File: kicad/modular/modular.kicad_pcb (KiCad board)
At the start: 2 copper layers, 50 x 36 mm, 55 parts, among them J1 CONN_PWR, J2 HEADER, J3 HEADER, U1 LM317, U2 LM337, U3 OPA4197, U4 REF5010

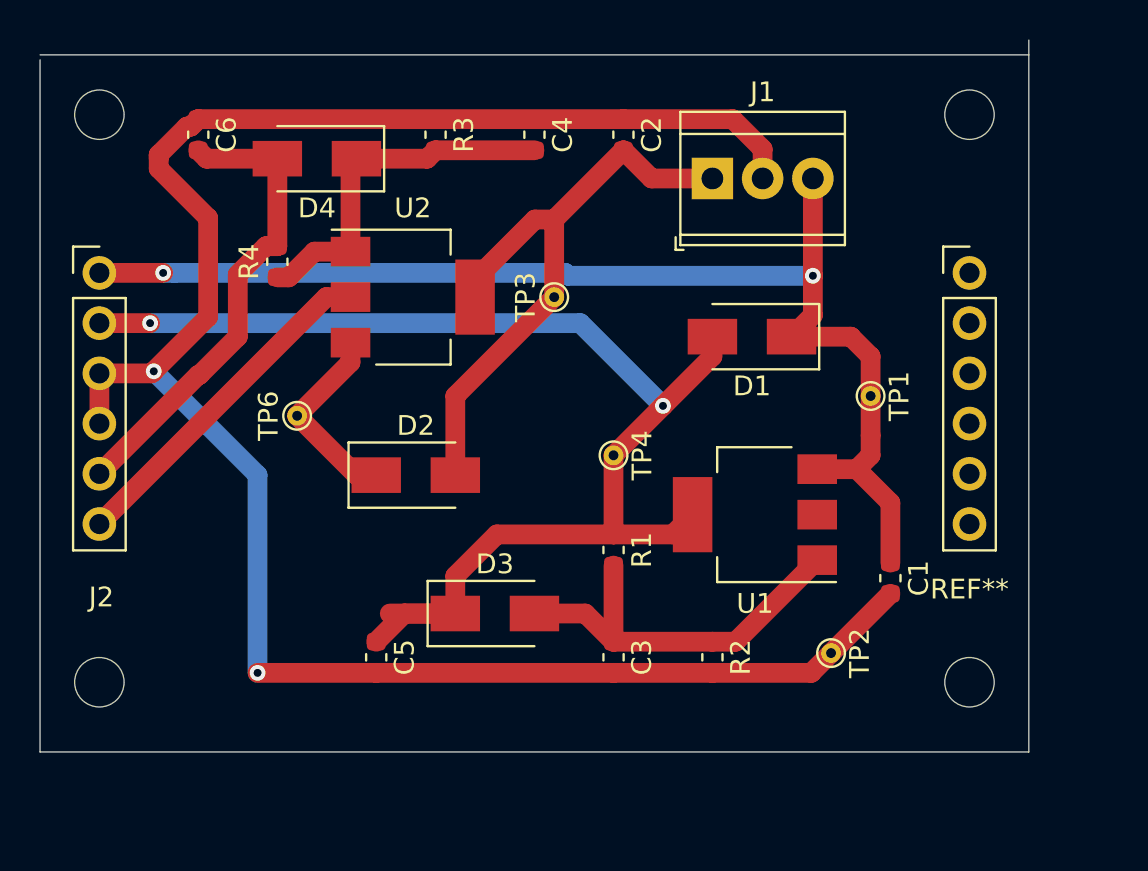
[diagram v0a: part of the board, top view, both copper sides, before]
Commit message: completed pcb design of power board
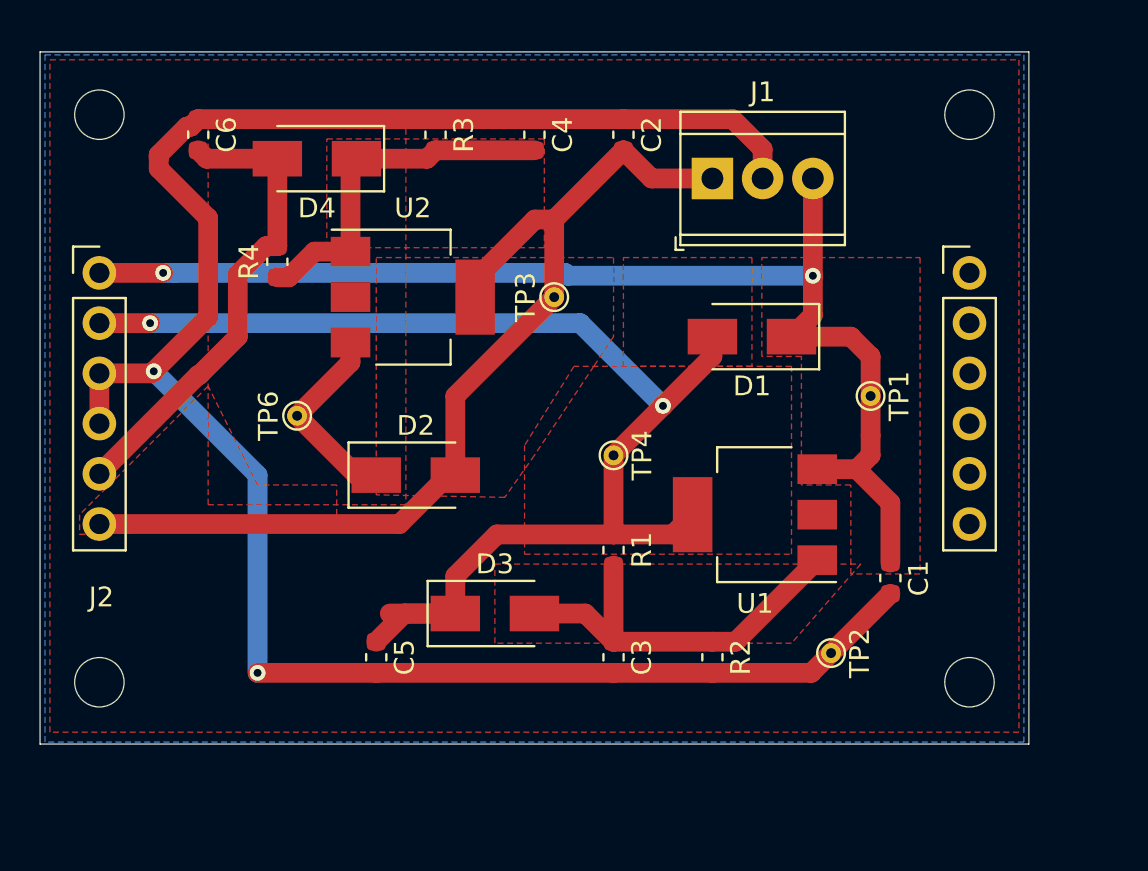
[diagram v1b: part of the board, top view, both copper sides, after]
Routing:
- net -15V: track 48.6 -> 50.2 mm
- added copper zone on F.Cu, net +12V
- added copper zone on F.Cu, net +15V
- added copper zone on F.Cu, net -12V
- added copper zone on F.Cu, net -15V
- added copper zone on B.Cu, net GND
- added copper zone on F.Cu, net GND
- added copper zone on F.Cu, net Net-(C3-Pad1)
- added copper zone on F.Cu, net Net-(C4-Pad2)
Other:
- board size 50 x 36 mm -> 50 x 35 mm
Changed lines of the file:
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@@
     (thickness 1.6)
     (drawings 4)
-    (tracks 102)
+    (tracks 103)
     (zones 0)
     (modules 55)
@@
   (layers
     (0 F.Cu signal)
-    (31 B.Cu signal)
+    (31 B.Cu signal hide)
     (32 B.Adhes user)
     (33 F.Adhes user)
@@
       (effects (font (size 1 1) (thickness 0.15)))
     )
-    (fp_text user REF** (at 44 16) (layer F.SilkS)
-      (effects (font (size 1 1) (thickness 0.15)))
-    )
     (fp_text user %R (at 0.3 -8) (layer F.Fab)
       (effects (font (size 1 1) (thickness 0.15)))
@@
     )
   )
-  (gr_line (start 40 26.75) (end 90 26.75) (layer Edge.Cuts) (width 0.05))
-  (gr_line (start 40 62) (end 40 27) (layer Edge.Cuts) (width 0.05))
-  (gr_line (start 90 62) (end 40 62) (layer Edge.Cuts) (width 0.05))
-  (gr_line (start 90 26) (end 90 62) (layer Edge.Cuts) (width 0.05))
+  (gr_line (start 40 26.6) (end 90 26.6) (layer Edge.Cuts) (width 0.05))
+  (gr_line (start 40 61.6) (end 40 26.6) (layer Edge.Cuts) (width 0.05))
+  (gr_line (start 90 61.6) (end 40 61.6) (layer Edge.Cuts) (width 0.05))
+  (gr_line (start 90 26.6) (end 90 61.6) (layer Edge.Cuts) (width 0.05))
   (segment (start 81.3 47.7) (end 82 47) (width 1) (layer F.Cu) (net 1))
   (segment (start 79.3 47.7) (end 81.3 47.7) (width 1) (layer F.Cu) (net 1))
@@
   (segment (start 70.925 33) (end 69.5 31.575) (width 1) (layer F.Cu) (net 3))
   (segment (start 74 33) (end 70.925 33) (width 1) (layer F.Cu) (net 3))
-  (segment (start 54.475001 39) (end 55.7 39) (width 1) (layer F.Cu) (net 3))
-  (segment (start 43 50.475001) (end 54.475001 39) (width 1) (layer F.Cu) (net 3))
+  (segment (start 58.174999 50.475001) (end 60.65 48) (width 1) (layer F.Cu) (net 3))
+  (segment (start 60.65 48) (end 61 48) (width 1) (layer F.Cu) (net 3))
+  (segment (start 43 50.475001) (end 58.174999 50.475001) (width 1) (layer F.Cu) (net 3))
   (segment (start 69 52.575) (end 69 56.425) (width 1) (layer F.Cu) (net 4))
   (segment (start 69 56.425) (end 74 56.425) (width 1) (layer F.Cu) (net 4))
@@
   (segment (start 51.425 36.425) (end 52 36.425) (width 1) (layer F.Cu) (net 7))
   (segment (start 50 41) (end 50 37.85) (width 1) (layer F.Cu) (net 7))
+  (zone (net 2) (net_name GND) (layer B.Cu) (hatch edge 0.508)
+    (connect_pads (clearance 0.508))
+    (min_thickness 0.254)
+    (fill yes (arc_segments 32) (thermal_gap 0.508) (thermal_bridge_width 0.508))
+    (polygon
+      (pts
+        (xy 40.25 26.75) (xy 89.75 26.75) (xy 89.75 61.5) (xy 40.25 61.5)
+      )
+    )
+  )
+  (zone (net 5) (net_name "Net-(C4-Pad2)") (layer F.Cu) (hatch edge 0.508)
+    (priority 5)
+    (connect_pads (clearance 0.508))
+    (min_thickness 0.254)
+    (fill yes (arc_segments 32) (thermal_gap 0.508) (thermal_bridge_width 0.508))
+    (polygon
+      (pts
+        (xy 54.5 31) (xy 65.5 31) (xy 65.5 36.5) (xy 54.5 36.5)
+      )
+    )
+  )
+  (zone (net 3) (net_name -15V) (layer F.Cu) (hatch edge 0.508)
+    (priority 4)
+    (connect_pads (clearance 0.508))
+    (min_thickness 0.254)
+    (fill yes (arc_segments 32) (thermal_gap 0.508) (thermal_bridge_width 0.508) (smoothing chamfer))
+    (polygon
+      (pts
+        (xy 57 37) (xy 69 37) (xy 69 41) (xy 68 42.5) (xy 65 47)
+        (xy 63.5 49.125) (xy 57 49)
+      )
+    )
+  )
+  (zone (net 4) (net_name "Net-(C3-Pad1)") (layer F.Cu) (hatch edge 0.508)
+    (priority 5)
+    (connect_pads (clearance 0.508))
+    (min_thickness 0.254)
+    (fill yes (arc_segments 32) (thermal_gap 0.508) (thermal_bridge_width 0.508) (smoothing chamfer))
+    (polygon
+      (pts
+        (xy 63 52.5) (xy 81.5 52.5) (xy 78 56.5) (xy 63 56.5)
+      )
+    )
+  )
+  (zone (net 6) (net_name +12V) (layer F.Cu) (hatch edge 0.508)
+    (priority 2)
+    (connect_pads (clearance 0.508))
+    (min_thickness 0.254)
+    (fill yes (arc_segments 32) (thermal_gap 0.508) (thermal_bridge_width 0.508) (smoothing chamfer))
+    (polygon
+      (pts
+        (xy 78 52) (xy 78 42.5) (xy 76 42.5) (xy 67 42.5) (xy 64.5 46.5)
+        (xy 64.5 52)
+      )
+    )
+  )
+  (zone (net 6) (net_name +12V) (layer F.Cu) (hatch edge 0.508)
+    (priority 2)
+    (connect_pads (clearance 0.508))
+    (min_thickness 0.254)
+    (fill yes (arc_segments 32) (thermal_gap 0.508) (thermal_bridge_width 0.508) (smoothing chamfer))
+    (polygon
+      (pts
+        (xy 69.5 37) (xy 76 37) (xy 76 42.5) (xy 69.5 42.5)
+      )
+    )
+  )
+  (zone (net 1) (net_name +15V) (layer F.Cu) (hatch edge 0.508)
+    (priority 4)
+    (connect_pads (clearance 0.508))
+    (min_thickness 0.254)
+    (fill yes (arc_segments 32) (thermal_gap 0.508) (thermal_bridge_width 0.508) (smoothing chamfer))
+    (polygon
+      (pts
+        (xy 76.5 37) (xy 84.5 37) (xy 84.5 53) (xy 81 53) (xy 81 48.5)
+        (xy 78.5 48.5) (xy 78.5 42) (xy 76.5 42)
+      )
+    )
+  )
+  (zone (net 2) (net_name GND) (layer F.Cu) (hatch edge 0.508)
+    (connect_pads (clearance 0.508))
+    (min_thickness 0.254)
+    (fill yes (arc_segments 32) (thermal_gap 0.508) (thermal_bridge_width 0.508) (smoothing chamfer))
+    (polygon
+      (pts
+        (xy 40.5 27) (xy 89.5 27) (xy 89.5 61) (xy 40.5 61)
+      )
+    )
+  )
+  (zone (net 7) (net_name -12V) (layer F.Cu) (hatch edge 0.508)
+    (priority 10)
+    (connect_pads (clearance 0.508))
+    (min_thickness 0.254)
+    (fill yes (arc_segments 32) (thermal_gap 0.508) (thermal_bridge_width 0.508) (smoothing chamfer))
+    (polygon
+      (pts
+        (xy 48.5 30) (xy 58.5 30) (xy 58.5 49.5) (xy 48.5 49.5)
+      )
+    )
+  )
+  (zone (net 3) (net_name -15V) (layer F.Cu) (hatch edge 0.508)
+    (priority 1)
+    (connect_pads (clearance 0.508))
+    (min_thickness 0.254)
+    (fill yes (arc_segments 32) (thermal_gap 0.508) (thermal_bridge_width 0.508) (smoothing chamfer))
+    (polygon
+      (pts
+        (xy 42 51) (xy 55 50.5) (xy 55 48.5) (xy 51 48.5) (xy 48.5 43.5)
+        (xy 42 50)
+      )
+    )
+  )
 )

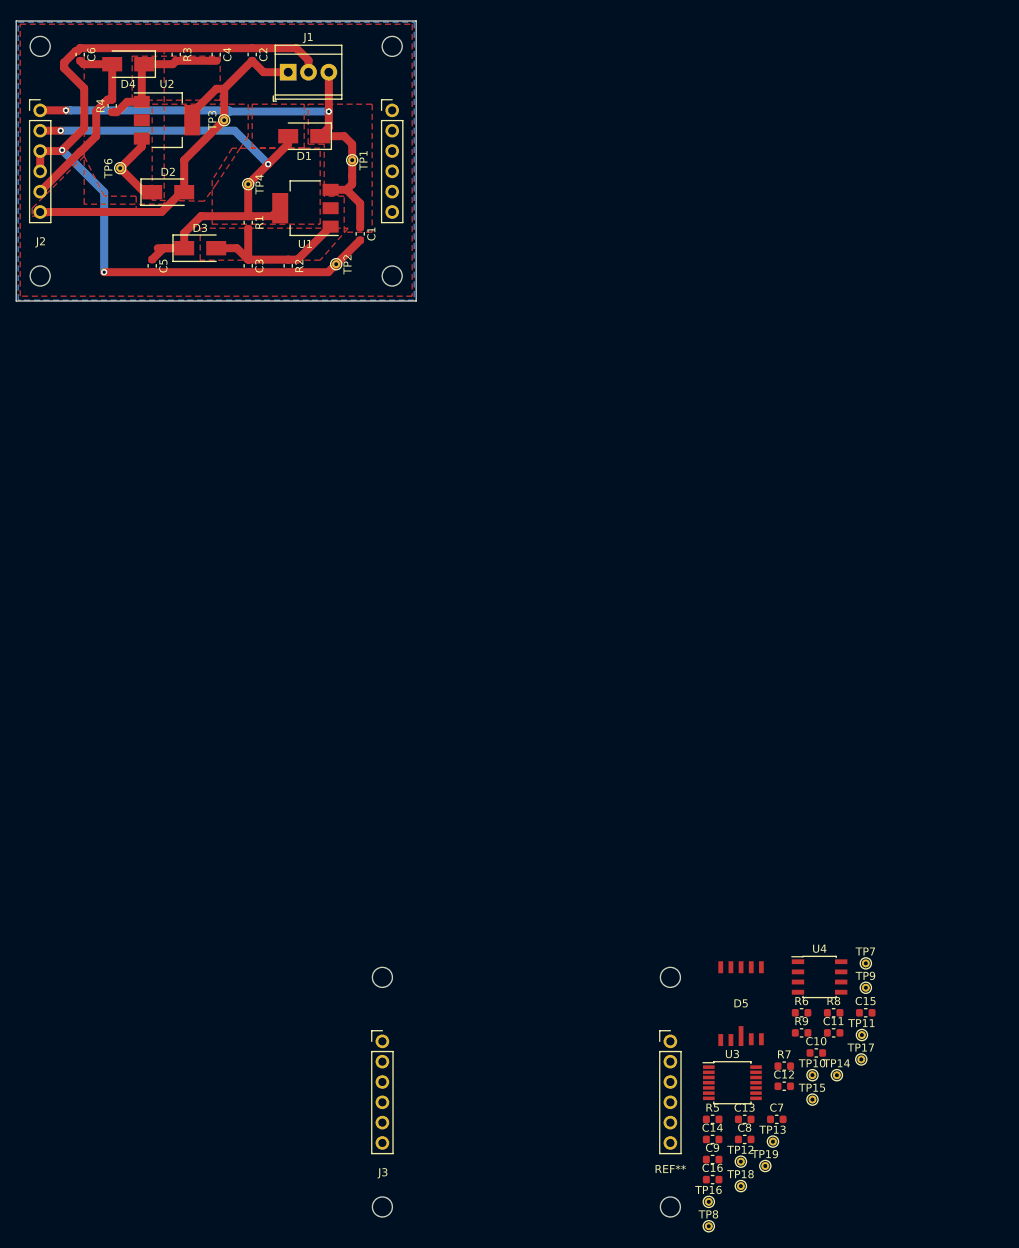
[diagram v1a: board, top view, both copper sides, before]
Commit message: updated detector board footprints, added edge cuts
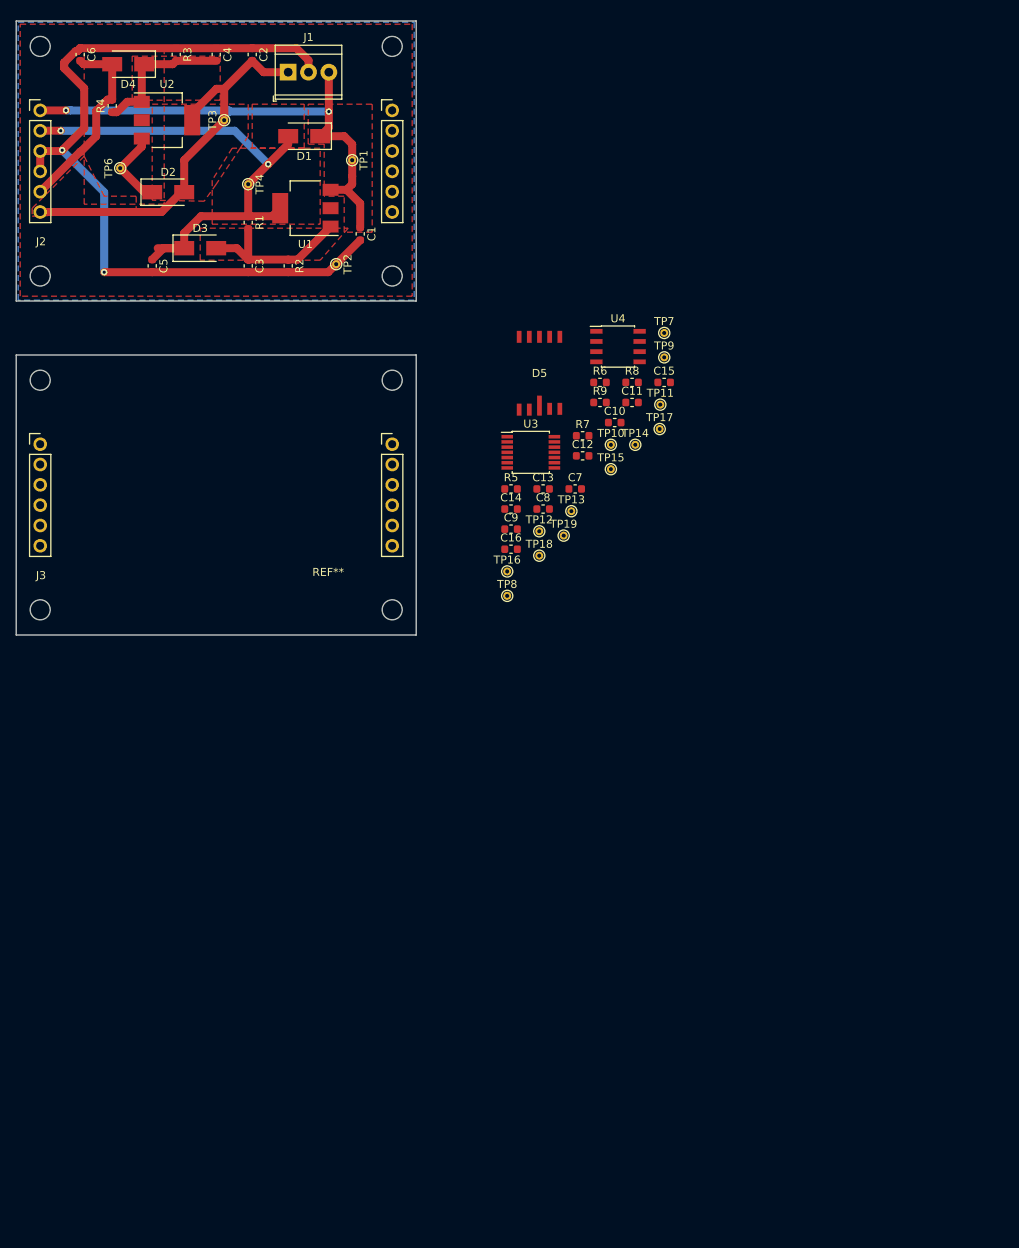
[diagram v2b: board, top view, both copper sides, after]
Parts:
- J2: value HEADER -> Power
- moved J3 86.0 mm to (43.0, 79.5)
- moved D5 82.7 mm to (105.4, 70.6)
- moved TP7 82.7 mm to (121.0, 65.6)
- moved C10 82.7 mm to (114.8, 76.8)
- moved C11 82.7 mm to (117.0, 74.3)
- moved C13 82.7 mm to (105.9, 85.1)
- moved C16 82.7 mm to (101.9, 92.6)
- moved C7 82.7 mm to (109.9, 85.1)
- moved R5 82.7 mm to (101.9, 85.1)
- moved R9 82.7 mm to (113.0, 74.3)
- moved TP13 82.7 mm to (109.4, 87.9)
- moved TP15 82.7 mm to (114.3, 82.6)
- moved TP16 82.7 mm to (101.4, 95.4)
- moved TP18 82.7 mm to (105.4, 93.4)
- moved TP9 82.7 mm to (121.0, 68.6)
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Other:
- board size 50 x 35 mm -> 50 x 76.8 mm

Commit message: completed detector board
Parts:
- removed TP11: I1, TestPoint:TestPoint_THTPad_D1.0mm_Drill0.5mm
- removed TP12: I3, TestPoint:TestPoint_THTPad_D1.0mm_Drill0.5mm
- removed TP14: U1, TestPoint:TestPoint_THTPad_D1.0mm_Drill0.5mm
- removed TP15: U3, TestPoint:TestPoint_THTPad_D1.0mm_Drill0.5mm
- removed TP16: I2, TestPoint:TestPoint_THTPad_D1.0mm_Drill0.5mm
- removed TP17: I4, TestPoint:TestPoint_THTPad_D1.0mm_Drill0.5mm
- removed TP18: X2, TestPoint:TestPoint_THTPad_D1.0mm_Drill0.5mm
- removed TP19: U4, TestPoint:TestPoint_THTPad_D1.0mm_Drill0.5mm
- J2: value Power -> HEADER
- TP7: value +15V -> +12V
- TP8: value -15V -> -12V
- moved TP7 73.8 mm to (47.7, 74.4)
- moved C15 69.5 mm to (54.5, 92.0), turned to 180 degrees
- moved R8 65.2 mm to (54.4, 90.2), turned to 180 degrees
- moved R6 63.3 mm to (50.3, 80.2)
- moved R7 61.7 mm to (50.2, 90.2)
- moved R9 58.8 mm to (54.4, 80.2), turned to 180 degrees
- moved C13 56.0 mm to (50.3, 78.3)
- moved C8 54.8 mm to (52.4, 76.0), turned to 270 degrees
- moved TP8 52.7 mm to (48.7, 99.4)
- moved U3 52.3 mm to (52.2, 85.2), turned to 270 degrees
- moved C14 51.8 mm to (50.2, 92.0)
- moved C9 49.7 mm to (52.3, 94.3), turned to 90 degrees
- moved C16 49.5 mm to (54.4, 78.3), turned to 180 degrees
- moved D5 46.1 mm to (61.7, 85.3)
- moved C10 46.1 mm to (70.5, 89.3), turned to 180 degrees
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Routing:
- net GND: track 103.7 -> 195.3 mm, vias 2 -> 6
- net /Detector/Y1: track 0.00 -> 51.6 mm, vias 0 -> 1
- net /Detector/X1: track 0.00 -> 50.7 mm, vias 0 -> 1
- net +15V: track 62.4 -> 109.1 mm
- net Net-(C12-Pad1): track 0.00 -> 43.0 mm
- net /Detector/Y2: track 0.00 -> 40.9 mm, vias 0 -> 2
- net /Detector/X2: track 0.00 -> 40.7 mm, vias 0 -> 1
- net Net-(C15-Pad2): track 0.00 -> 28.8 mm
- net -12V: track 34.3 -> 57.4 mm
- net Net-(C14-Pad2): track 0.00 -> 21.5 mm
- net +12V: track 65.4 -> 86.4 mm
- net Net-(C13-Pad2): track 0.00 -> 15.6 mm
- net Net-(C16-Pad2): track 0.00 -> 12.2 mm
- net Net-(C11-Pad1): track 0.00 -> 4.61 mm
- net Net-(C10-Pad1): track 0.00 -> 3.36 mm

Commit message: started redesign of pcb
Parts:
- removed TP10: BIAS, TestPoint:TestPoint_THTPad_D1.0mm_Drill0.5mm
- removed TP13: GND, TestPoint:TestPoint_THTPad_D1.0mm_Drill0.5mm
- removed TP4, TP7: +12V, TestPoint:TestPoint_THTPad_D1.0mm_Drill0.5mm
- removed TP6, TP8: -12V, TestPoint:TestPoint_THTPad_D1.0mm_Drill0.5mm
- removed TP9: +15V, TestPoint:TestPoint_THTPad_D1.0mm_Drill0.5mm
- TP1: value +15V -> +12V
- TP2: value GND -> -12V
- TP3: value -15V -> BIAS
- moved TP3 125.0 mm to (161.7, 119.4), turned to 0 degrees
- moved C13 117.4 mm to (156.0, 129.2)
- moved R7 111.6 mm to (158.2, 118.6)
- moved R9 111.5 mm to (158.2, 121.1), turned to 0 degrees
- moved C6 108.8 mm to (129.1, 103.3), turned to 90 degrees
- moved TP2 108.0 mm to (132.1, 151.6), turned to 0 degrees
- moved TP1 107.7 mm to (161.7, 116.4), turned to 0 degrees
- moved U3 107.7 mm to (149.5, 131.3), turned to 0 degrees
- moved C8 107.2 mm to (128.6, 151.4), turned to 0 degrees
- moved C15 106.5 mm to (158.2, 116.1), turned to 0 degrees
- moved R8 106.3 mm to (147.1, 142.3), turned to 0 degrees
- moved R6 102.9 mm to (124.6, 151.4)
- moved D4 98.9 mm to (126.2, 99.6), turned to 90 degrees
- moved C7 98.6 mm to (160.0, 123.7), turned to 0 degrees
- moved R3 96.2 mm to (123.3, 103.3), turned to 90 degrees
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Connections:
- TP1 pad 1: +15V -> +12V
- TP2 pad 1: GND -> -12V
- TP3 pad 1: -15V -> Net-(C12-Pad1)
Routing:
- net GND: track 195.3 -> 85.4 mm, vias 6 -> 3
- net +15V: track 109.1 -> 31.2 mm, vias 2 -> 0
- net /Detector/Y1: track 51.6 -> 0.00 mm, vias 1 -> 0
- net /Detector/X1: track 50.7 -> 0.00 mm, vias 1 -> 0
- net Net-(C12-Pad1): track 43.0 -> 0.00 mm
- net /Detector/Y2: track 40.9 -> 0.00 mm, vias 2 -> 0
- net /Detector/X2: track 40.7 -> 0.00 mm, vias 1 -> 0
- net Net-(C15-Pad2): track 28.8 -> 0.00 mm
- net Net-(C14-Pad2): track 21.5 -> 0.00 mm
- net +12V: track 86.4 -> 65.4 mm, vias 2 -> 0
- net Net-(C13-Pad2): track 15.6 -> 0.00 mm
- net -15V: track 50.2 -> 36.3 mm
- net Net-(C16-Pad2): track 12.2 -> 0.00 mm
- net Net-(C4-Pad2): track 18.2 -> 11.1 mm
- net Net-(C3-Pad1): track 20.4 -> 14.9 mm
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- removed copper zone on F.Cu, net +12V
- removed copper zone on F.Cu, net +15V
- removed copper zone on F.Cu, net -12V
- removed copper zone on F.Cu, net -15V
- removed copper zone on B.Cu, net GND
- removed copper zone on F.Cu, net GND
- removed copper zone on F.Cu, net Net-(C3-Pad1)
- removed copper zone on F.Cu, net Net-(C4-Pad2)
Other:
- board outline removed
